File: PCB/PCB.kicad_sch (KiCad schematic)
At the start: 3 parts, among them U1 Pico

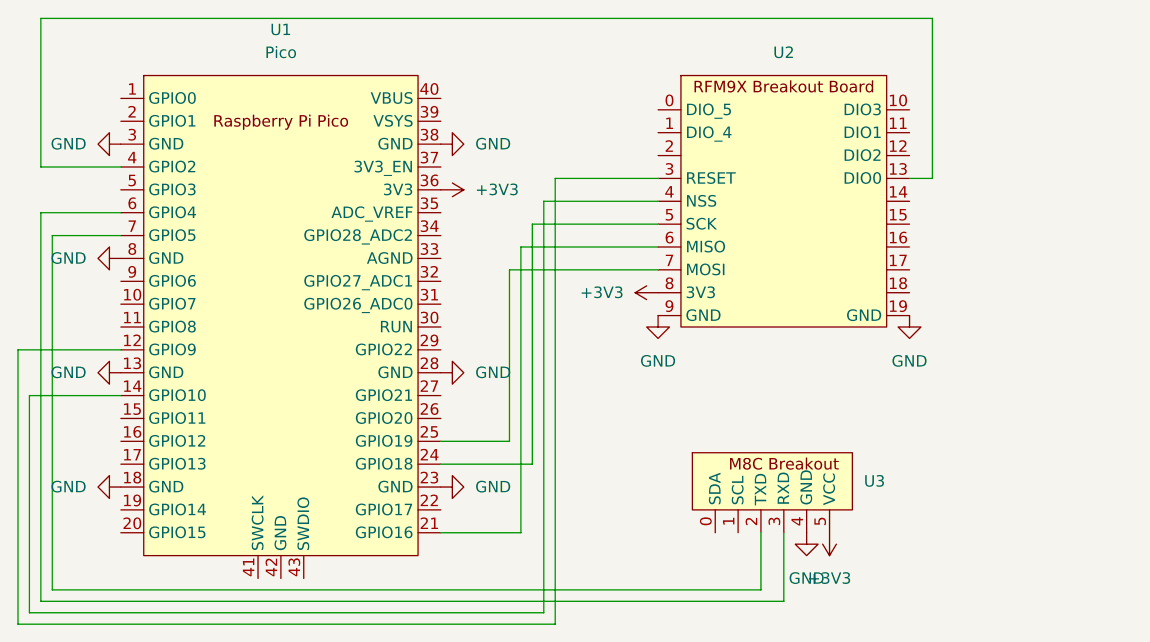
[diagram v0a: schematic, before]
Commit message: Updated PCB to use SMT RFM9X
PCB now on v1.1, currently untested
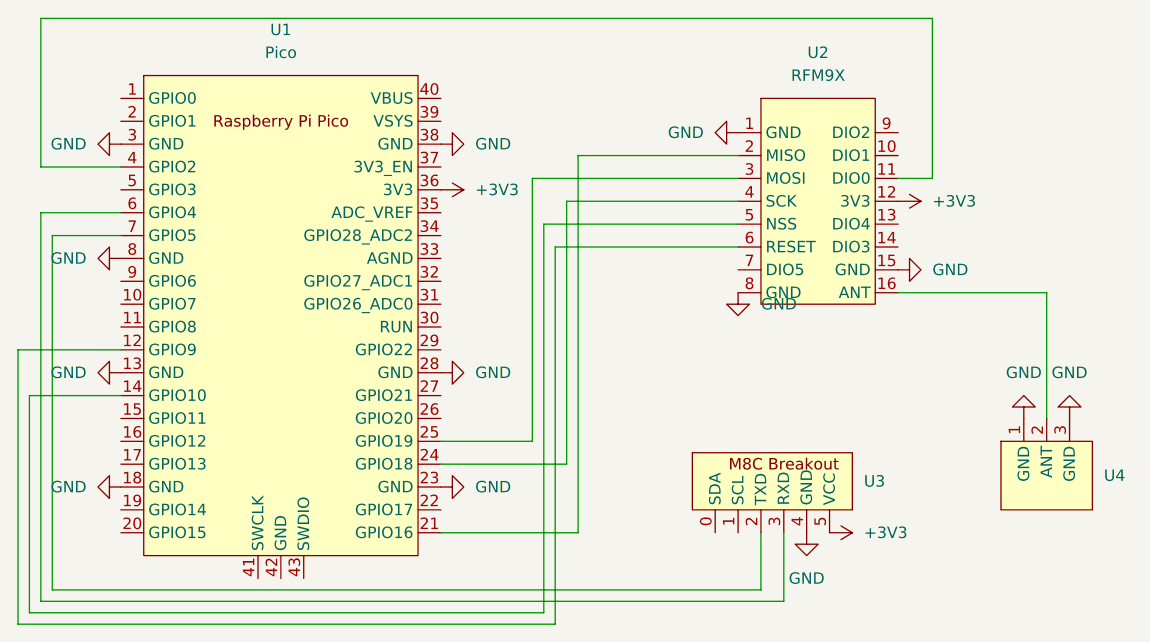
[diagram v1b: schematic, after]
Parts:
- removed U2: ~, RFM9X-Breakout:RFM9X, symbol RFM9X-Breakout:RFM9X
- added U2: RFM9X, RFM9X:RFM9X, symbol RFM9X:RFM9X
- added U4: ~, RFM9X:Antenna, symbol RFM9X:Antenna
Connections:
- net +3V3: now also U2.12 (3V3)
- net GND: now also U2.1 (GND), U2.15 (GND), U2.8 (GND), U4.1 (GND), U4.3 (GND)
- net at U1.12 (GPIO9): now also U2.6 (RESET)
- net at U1.14 (GPIO10): now also U2.5 (NSS)
- net at U1.21 (GPIO16): now also U2.2 (MISO)
- net at U1.24 (GPIO18): now also U2.4 (SCK)
- net at U1.25 (GPIO19): now also U2.3 (MOSI)
- net at U1.4 (GPIO2): now also U2.11 (DIO0)
- new net: U2.16 (ANT), U4.2 (ANT)
